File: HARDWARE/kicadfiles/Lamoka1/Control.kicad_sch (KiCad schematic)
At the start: 0 parts

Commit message: Better multiple color model for Lamoka1-DEV-Brain
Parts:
- added P1: USB_C_Plug_USB2.0, symbol Connector:USB_C_Plug_USB2.0
- added U4: RP2354A, Package_DFN_QFN:QFN-60-1EP_7x7mm_P0.4mm_EP3.4x3.4mm, symbol MCU_RaspberryPi:RP2354A
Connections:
- new net: U4.1 (IOVDD), U4.11 (IOVDD), U4.20 (IOVDD), U4.30 (IOVDD), U4.38 (IOVDD), U4.45 (IOVDD)
- new net: U4.23 (DVDD), U4.39 (DVDD), U4.6 (DVDD)
- new net: P1.A1 (GND), P1.A12 (GND), P1.B1 (GND), P1.B12 (GND)
- new net: P1.A4 (VBUS), P1.A9 (VBUS), P1.B4 (VBUS), P1.B9 (VBUS)

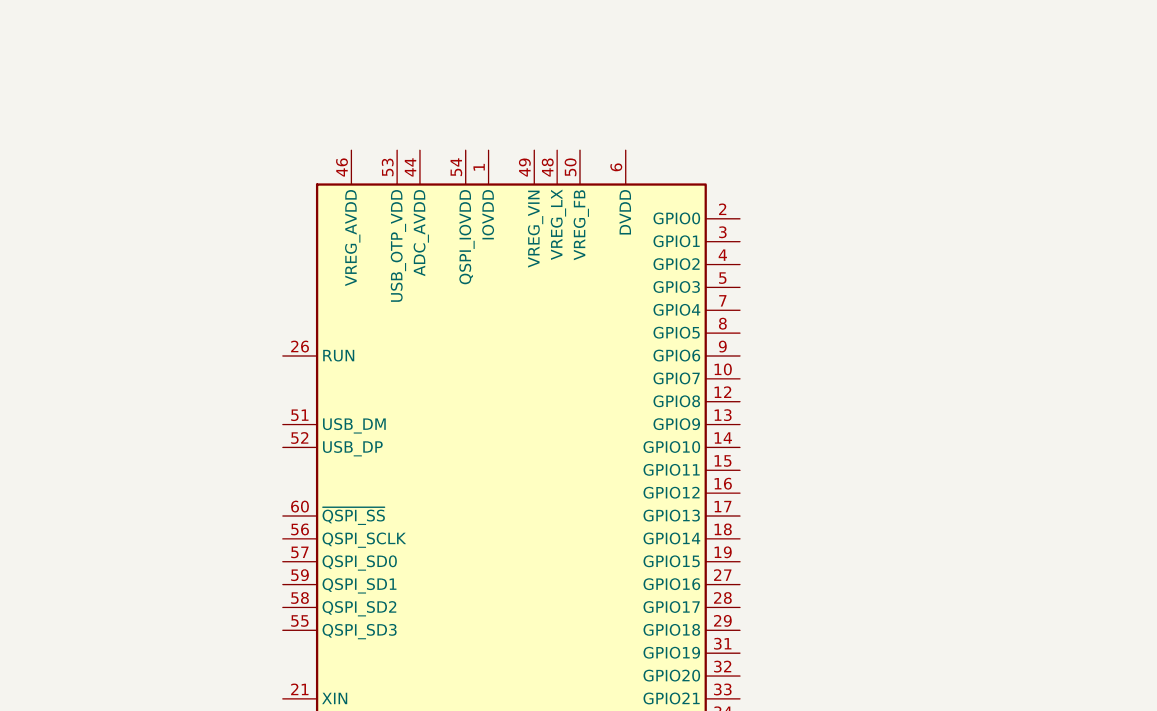
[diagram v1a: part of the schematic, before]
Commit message: ADD values to Lamoka1 charging section, and Lamoka1 control button
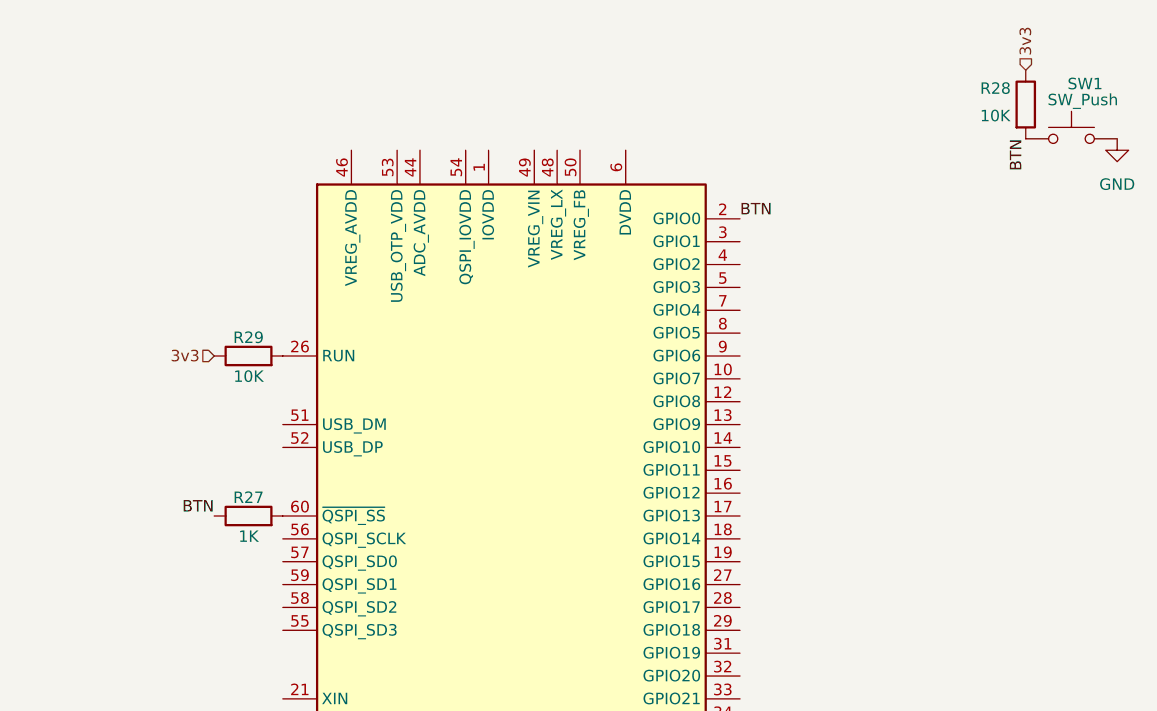
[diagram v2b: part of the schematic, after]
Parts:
- added R27: 1K, symbol Device:R
- added R28, R29: 10K, symbol Device:R
- added SW1: SW_Push, symbol Switch:SW_Push
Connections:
- net BTN: now reaches U4.2 (GPIO0)
- net BTN: now also R27.1, R28.2, SW1.1
- net at U4.26 (RUN): now also R29.2
- net at U4.60 (~{QSPI_SS}): now also R27.2
- new net 3v3: R28.1, R29.1
- new net GND: SW1.2

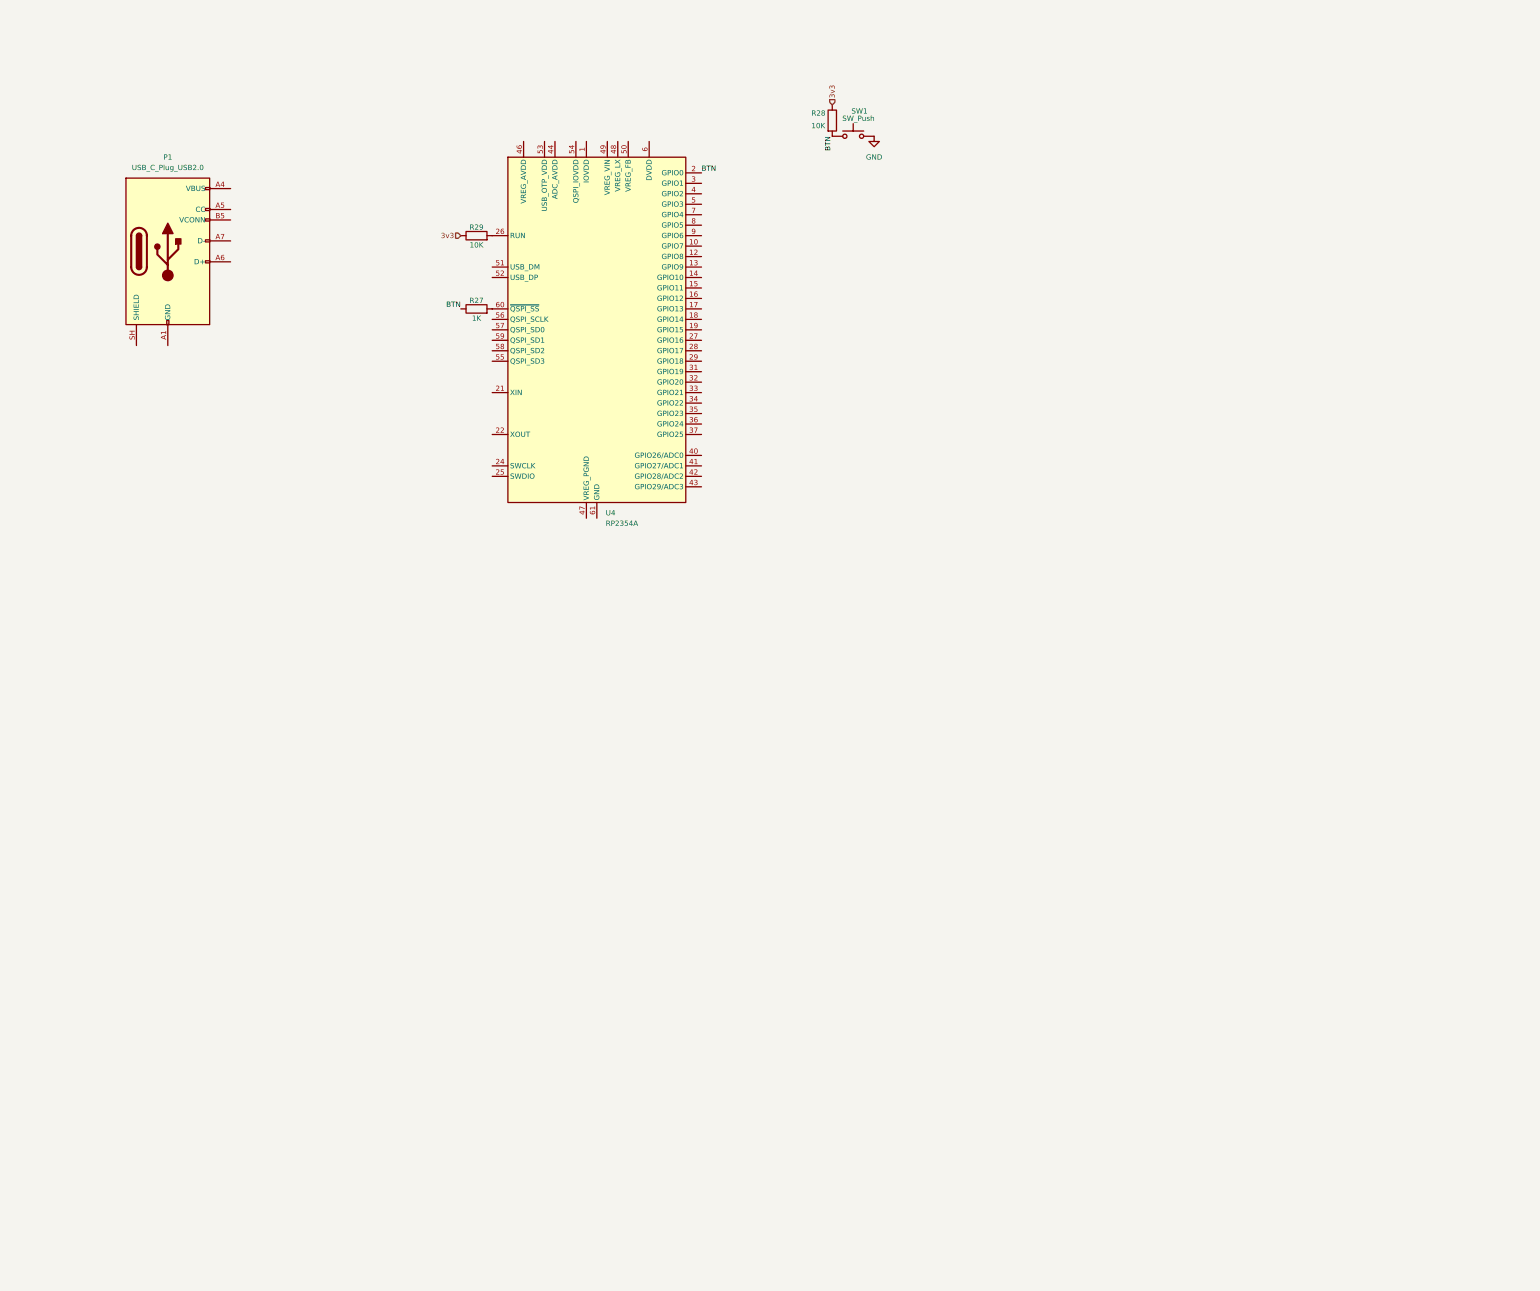
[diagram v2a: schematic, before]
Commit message: New PIE version, misc hardware schem improments for Lamoka1
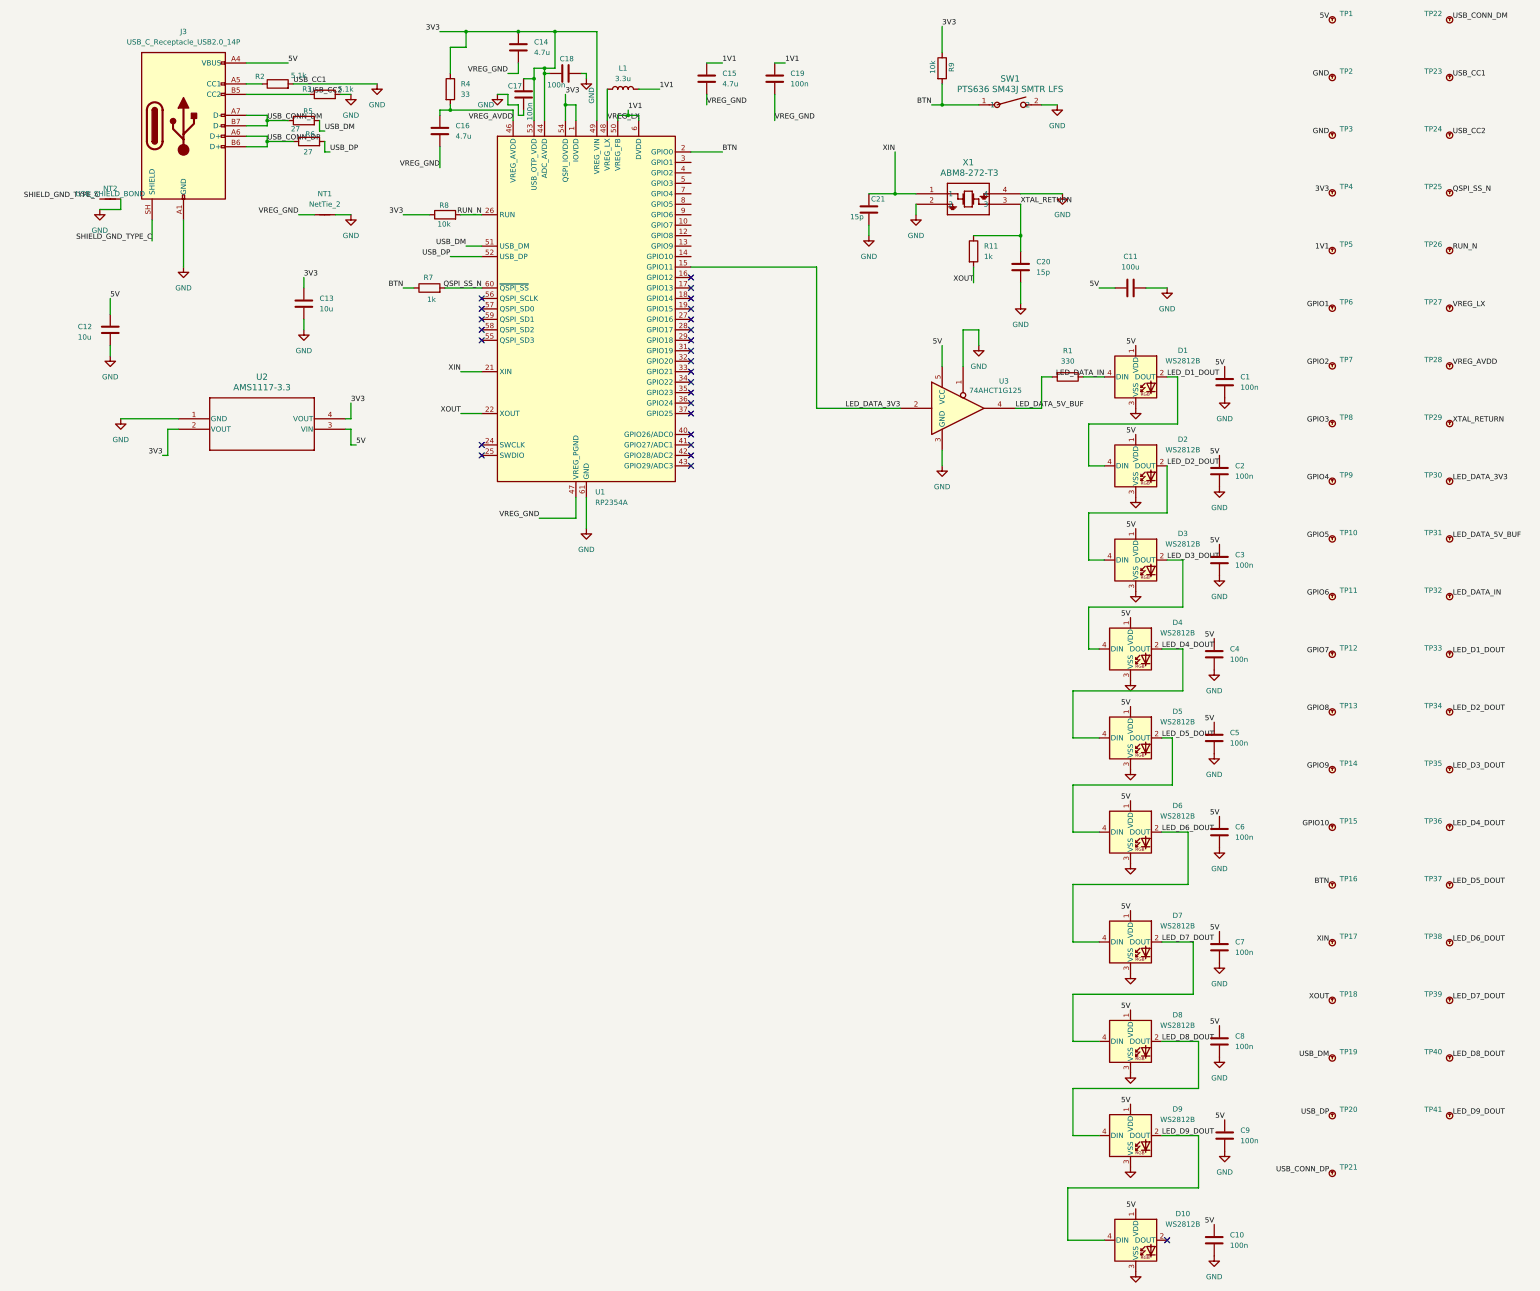
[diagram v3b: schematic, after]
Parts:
- removed P1: USB_C_Plug_USB2.0, symbol Connector:USB_C_Plug_USB2.0
- removed R27: 1K, symbol Device:R
- removed R28, R29: 10K, symbol Device:R
- removed SW1: SW_Push, symbol Switch:SW_Push
- removed U4: RP2354A, Package_DFN_QFN:QFN-60-1EP_7x7mm_P0.4mm_EP3.4x3.4mm, symbol MCU_RaspberryPi:RP2354A
- added C1, C10, C17, C18, C19, C2, C3, C4, C5, C6, C7, C8, C9: 100n, components:CAP_0402_SAM, symbol Device:C
- added C11: 100u, Capacitor_SMD:C_1206_3216Metric, symbol Device:C
- added C12, C13: 10u, components:CAP_CL_05_SAM, symbol Device:C
- added C14, C15, C16: 4.7u, components:CAP_0603_CL10A_1P6XP8_SAM, symbol Device:C
- added C20, C21: 15p, Capacitor_SMD:C_0402_1005Metric, symbol Device:C
- added D1, D10, D2, D3, D4, D5, D6, D7, D8, D9: WS2812B, LED_SMD:LED_WS2812B_PLCC4_5.0x5.0mm_P3.2mm, symbol LED:WS2812B
- added J3: USB_C_Receptacle_USB2.0_14P, Connector_USB:USB_C_Receptacle_HRO_TYPE-C-31-M-12, symbol Connector:USB_C_Receptacle_USB2.0_14P
- added L1: 3.3u, components:AOTAB201610S3R3101T, symbol Device:L
- added NT1: NetTie_2, NetTie:NetTie-2_SMD_Pad0.5mm, symbol Device:NetTie_2
- added NT2: USB_SHIELD_BOND, symbol Device:NetTie_2
- added R1: 330, Resistor_SMD:R_0603_1608Metric, symbol Device:R
- added R11, R7: 1k, components:RC0402N_PAN, symbol Device:R
- added R2, R3: 5.1k, components:RC0603N_YAG, symbol Device:R
- added R4: 33, Resistor_SMD:R_0603_1608Metric, symbol Device:R
- added R5, R6: 27, Resistor_SMD:R_0603_1608Metric, symbol Device:R
- added R8, R9: 10k, components:RES_CRCW_0603, symbol Device:R
- added SW1: PTS636 SM43J SMTR LFS, components:SW_PTS636_CNK, symbol 2026-07-07_01-19-01:PTS636_SM43J_SMTR_LFS
- added TP1, TP10, TP11, TP12, TP13, TP14, TP15, TP16, TP17, TP18, TP19, TP2, TP20, TP21, TP3, TP4, TP5, TP6, TP7, TP8, TP9: Tomachie_TP_E, Pads:TPS127, symbol Pads:Tomachie_TP_E
- added TP22, TP23, TP24, TP25, TP26, TP27, TP28, TP29, TP30, TP31, TP32, TP33, TP34, TP35, TP36, TP37, TP38, TP39, TP40, TP41: Tomachie_TP_W, Pads:TPS127, symbol Pads:Tomachie_TP_W
- added U1: RP2354A, Package_DFN_QFN:QFN-60-1EP_7x7mm_P0.4mm_EP3.4x3.4mm, symbol MCU_RaspberryPi:RP2354A
- added U2: AMS1117-3.3, components:SOT-223_UMW, symbol 2026-07-07_01-04-34:AMS1117-3.3
- added U3: 74AHCT1G125, Package_TO_SOT_SMD:SOT-23-5, symbol 74xGxx:74AHCT1G125
- added X1: ABM8-272-T3, components:ABM8-272-T3_ABR, symbol 2026-07-07_19-38-11:ABM8-272-T3
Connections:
- net BTN: now also R7.1, R9.2, SW1.1, TP16.1, U1.2 (GPIO0)
- net GND: now also C1.2, C10.2, C11.2, C12.1, C13.2, C17.2, C18.2, C2.2, C20.2, C21.2, C3.2, C4.2, C5.2, C6.2, C7.2, C8.2, C9.2, D1.3 (VSS), D10.3 (VSS), D2.3 (VSS), D3.3 (VSS), D4.3 (VSS), D5.3 (VSS), D6.3 (VSS), D7.3 (VSS), D8.3 (VSS), D9.3 (VSS), J3.A1 (GND), J3.A12 (GND), J3.B1 (GND), J3.B12 (GND), NT1.2, NT2.2, R2.2, R3.2, SW1.2, TP2.1, TP23.1, TP3.1, U1.61 (GND), U2.1 (GND), U3.1, U3.3 (GND), X1.2, X1.4
- new net: J3.A5 (CC1), R2.1
- new net 1V1: C15.1, C19.1, L1.2, TP5.1, U1.23 (DVDD), U1.39 (DVDD), U1.50 (VREG_FB), U1.6 (DVDD)
- new net 3V3: C13.1, C14.1, C17.1, C18.1, R4.1, R8.1, R9.1, TP4.1, U1.1 (IOVDD), U1.11 (IOVDD), U1.20 (IOVDD), U1.30 (IOVDD), U1.38 (IOVDD), U1.44 (ADC_AVDD), U1.45 (IOVDD), U1.49 (VREG_VIN), U1.53 (USB_OTP_VDD), U1.54 (QSPI_IOVDD), U2.2 (VOUT), U2.4 (VOUT)
- new net 5V: C1.1, C10.1, C11.1, C12.2, C2.1, C3.1, C4.1, C5.1, C6.1, C7.1, C8.1, C9.1, D1.1 (VDD), D10.1 (VDD), D2.1 (VDD), D3.1 (VDD), D4.1 (VDD), D5.1 (VDD), D6.1 (VDD), D7.1 (VDD), D8.1 (VDD), D9.1 (VDD), J3.A4 (VBUS), J3.A9 (VBUS), J3.B4 (VBUS), J3.B9 (VBUS), TP1.1, U2.3 (VIN), U3.5 (VCC)
- new net GPIO1: TP6.1
- new net GPIO10: TP15.1
- new net GPIO2: TP7.1
- new net GPIO3: TP8.1
- new net GPIO4: TP9.1
- new net GPIO5: TP10.1
- new net GPIO6: TP11.1
- new net GPIO7: TP12.1
- new net GPIO8: TP13.1
- new net GPIO9: TP14.1
- new net LED_D1_DOUT: D1.2 (DOUT), D2.4 (DIN), TP33.1
- new net LED_D2_DOUT: D2.2 (DOUT), D3.4 (DIN), TP34.1
- new net LED_D3_DOUT: D3.2 (DOUT), D4.4 (DIN), TP35.1
- new net LED_D4_DOUT: D4.2 (DOUT), D5.4 (DIN), TP36.1
- new net LED_D5_DOUT: D5.2 (DOUT), D6.4 (DIN), TP37.1
- new net LED_D6_DOUT: D6.2 (DOUT), D7.4 (DIN), TP38.1
- new net LED_D7_DOUT: D7.2 (DOUT), D8.4 (DIN), TP39.1
- new net LED_D8_DOUT: D8.2 (DOUT), D9.4 (DIN), TP40.1
- new net LED_D9_DOUT: D10.4 (DIN), D9.2 (DOUT), TP41.1
- new net LED_DATA_3V3: TP30.1, U1.15 (GPIO11), U3.2
- new net LED_DATA_5V_BUF: R1.2, TP31.1, U3.4
- new net LED_DATA_IN: D1.4 (DIN), R1.1, TP32.1
- new net QSPI_SS_N: R7.2, TP25.1, U1.60 (~{QSPI_SS})
- new net RUN_N: R8.2, TP26.1, U1.26 (RUN)
- new net SHIELD_GND_TYPE_C: J3.SH (SHIELD), NT2.1
- new net USB_CC2: J3.B5 (CC2), R3.1, TP24.1
- new net USB_CONN_DM: J3.A7 (D-), J3.B7 (D-), R5.1, TP22.1
- new net USB_CONN_DP: J3.A6 (D+), J3.B6 (D+), R6.1, TP21.1
- new net USB_DM: R5.2, TP19.1, U1.51 (USB_DM)
- new net USB_DP: R6.2, TP20.1, U1.52 (USB_DP)
- new net VREG_AVDD: C16.1, R4.2, TP28.1, U1.46 (VREG_AVDD)
- new net VREG_GND: C14.2, C15.2, C16.2, C19.2, NT1.1, U1.47 (VREG_PGND)
- new net VREG_LX: L1.1, TP27.1, U1.48 (VREG_LX)
- new net XIN: C21.1, TP17.1, U1.21 (XIN), X1.1
- new net XOUT: R11.2, TP18.1, U1.22 (XOUT)
- new net XTAL_RETURN: C20.1, R11.1, TP29.1, X1.3
- no-connect marks 0 -> 26

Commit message: docs: Document prototype P1 schematic design improvements
Major updates to boost converter topology with LM5122 driver,
connect all section interfaces (charging, control), fix net connectivity.

This represents a near-complete functional schematic for the Lamoka1
inverter/charger system. All three main sections now have proper
interconnections for the RP2354A control implementation.
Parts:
- renumbered D10 to D13, D9 to D14
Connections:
- net I2C_SCL: now reaches U1.3 (GPIO1)
- net I2C_SDA: now reaches U1.4 (GPIO2)
- net CHG_CE: now reaches U1.5 (GPIO3)
- net CHG_INT: now reaches U1.7 (GPIO4)
- net SIGM: now reaches U1.8 (GPIO5)

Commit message: Revert "docs: Document prototype P1 schematic design improvements"
This reverts commit 9a36aaba68a23f8da8ed8c8f957268abdd88419f.
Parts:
- renumbered D13 to D10, D14 to D9
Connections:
- net CHG_CE: no longer names the net of U1.5 (GPIO3)
- net CHG_INT: no longer names the net of U1.7 (GPIO4)
- net I2C_SCL: no longer names the net of U1.3 (GPIO1)
- net I2C_SDA: no longer names the net of U1.4 (GPIO2)
- net SIGM: no longer names the net of U1.8 (GPIO5)

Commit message: re connect control
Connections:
- net I2C_SCL: now reaches U1.3 (GPIO1)
- net I2C_SDA: now reaches U1.4 (GPIO2)
- net CHG_CE: now reaches U1.5 (GPIO3)
- net CHG_INT: now reaches U1.7 (GPIO4)
- net SIGM: now reaches U1.8 (GPIO5)
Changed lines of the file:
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@@
+		)
+	)
+	(hierarchical_label "I2C_SDA"
+		(shape input)
+		(at 165.1 57.15 0)
+		(effects
+			(font
+				(size 1.27 1.27)
+			)
+			(justify left)
+		)
+	)
+	(hierarchical_label "I2C_SCL"
+		(shape input)
+		(at 165.1 54.61 0)
+		(effects
+			(font
+				(size 1.27 1.27)
+			)
+			(justify left)
+		)
+	)
+	(hierarchical_label "CHG_INT"
+		(shape input)
+		(at 165.1 62.23 0)
+		(effects
+			(font
+				(size 1.27 1.27)
+			)
+			(justify left)
+		)
+	)
+	(hierarchical_label "SIGM"
+		(shape input)
+		(at 165.1 64.77 0)
+		(effects
+			(font
+				(size 1.27 1.27)
+			)
+			(justify left)
+		)
+	)
+	(hierarchical_label "CHG_CE"
+		(shape input)
+		(at 165.1 59.69 0)
+		(effects
+			(font
+				(size 1.27 1.27)
+			)
+			(justify left)
 		)
 	)
